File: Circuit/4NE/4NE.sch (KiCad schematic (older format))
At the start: 30 parts, among them IC1 PIC16F18857-I_SP, J1 Conn_01x14_Female, J2 Conn_01x14_Female, J3 S8B-XH-A-1_LF__SN_, J4 S8B-XH-A-1_LF__SN_, U1 MAX485E

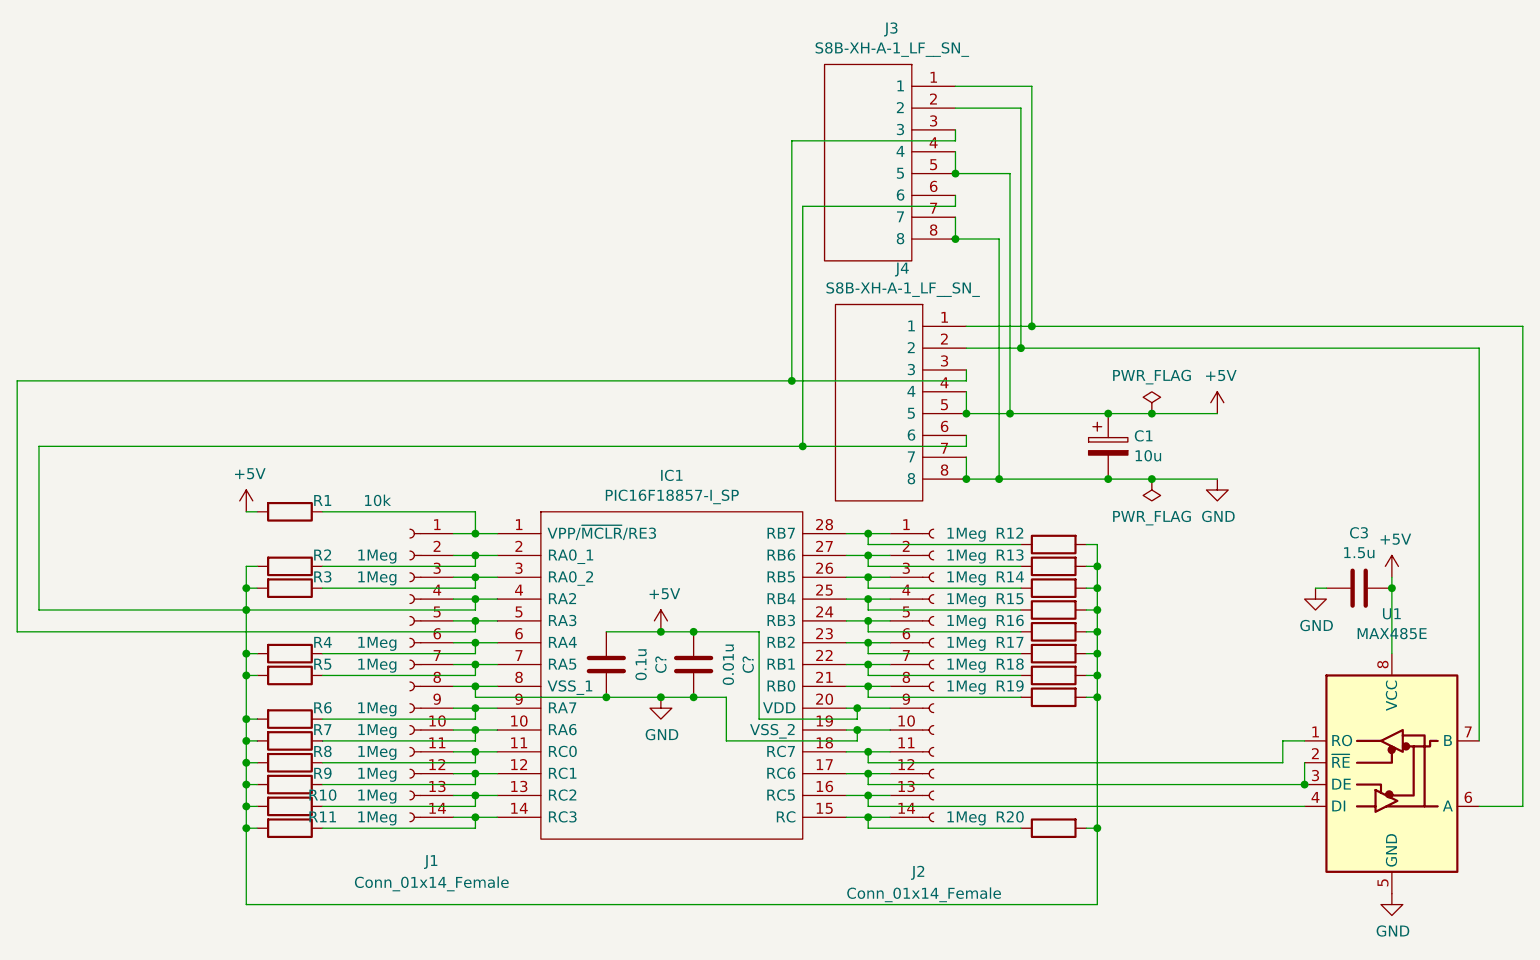
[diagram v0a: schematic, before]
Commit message: 8bit circuit (chip#0-5) complete
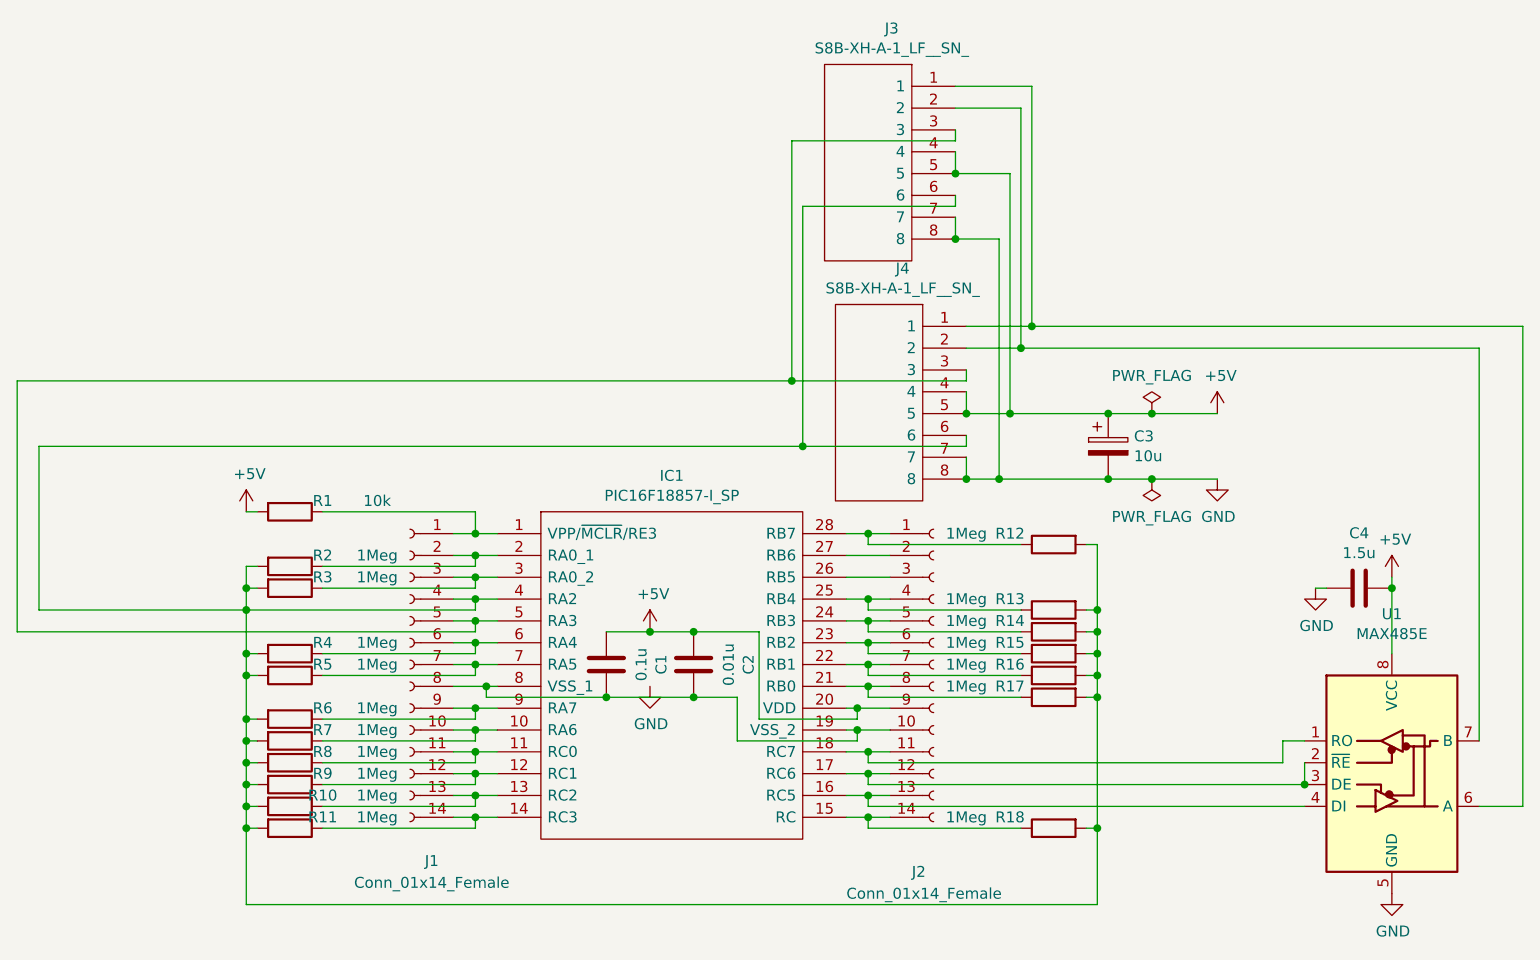
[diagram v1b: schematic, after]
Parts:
- removed C?: 0.1u, symbol Device:C
- removed C?: 0.01u, symbol Device:C
- removed R13, R14: 1Meg, symbol Device:R
- added C1: 0.1u, symbol Device:C
- added C2: 0.01u, symbol Device:C
- renumbered C1 to C3, C3 to C4, R15 to R13, R16 to R14, R17 to R15, R18 to R16, R19 to R17, R20 to R18
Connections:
- net +5V: now also C1.2, C2.2
- net GND: no longer IC1.19 (VSS_2), IC1.8 (VSS_1), J1.8 (Pin_8), J2.10 (Pin_10)
- new net: C1.1, C2.1, IC1.19 (VSS_2), IC1.8 (VSS_1), J1.8 (Pin_8), J2.10 (Pin_10)
